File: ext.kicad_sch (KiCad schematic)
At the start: 41 parts, among them J4 0826-1X1T-GH-F, J8 Conn_01x02_Male, J9 Conn_01x02_Male, U10 LTC6820HMS, U11 LTC6820HMS, U12 LTC6820HMS, U13 AP1117-33, U9 LTC6820HMS

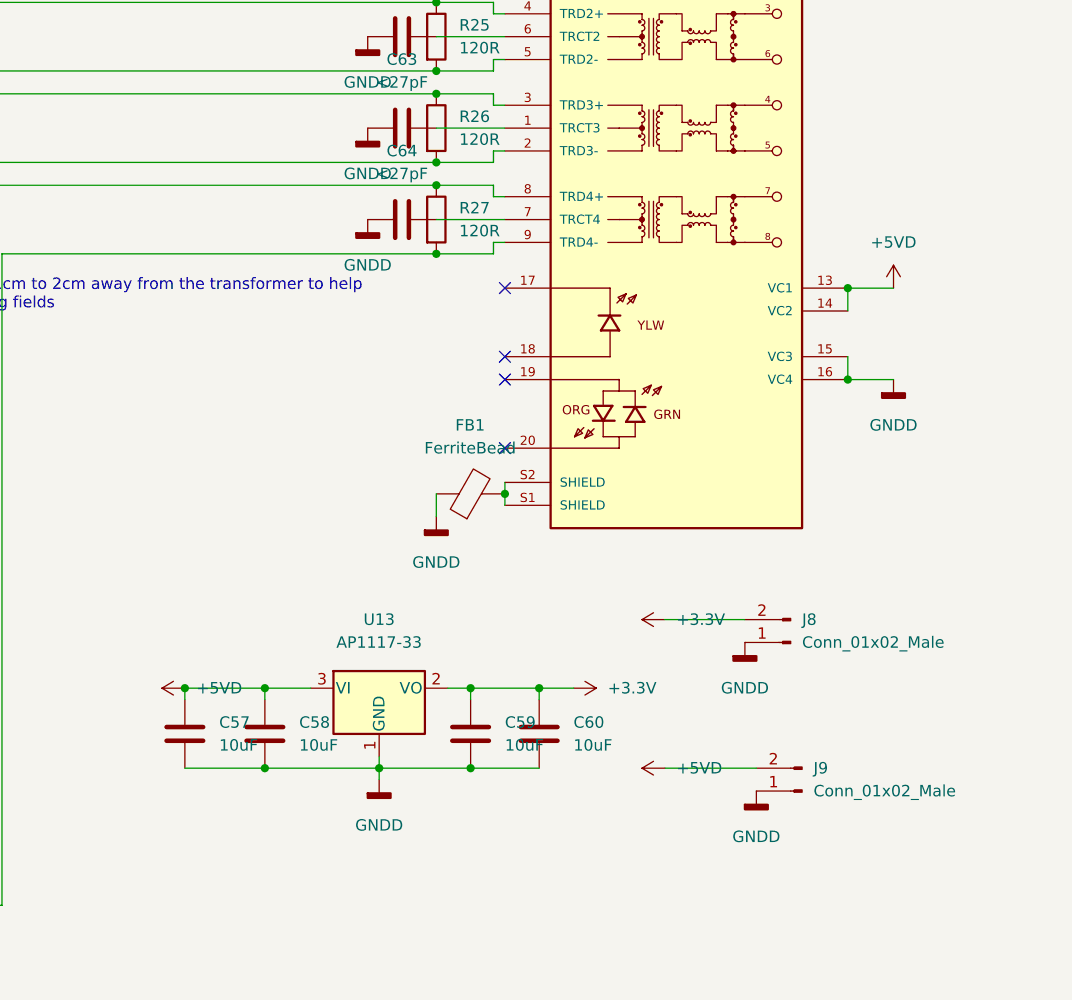
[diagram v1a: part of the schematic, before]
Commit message: remove 5V (now 3.3V) + tuning
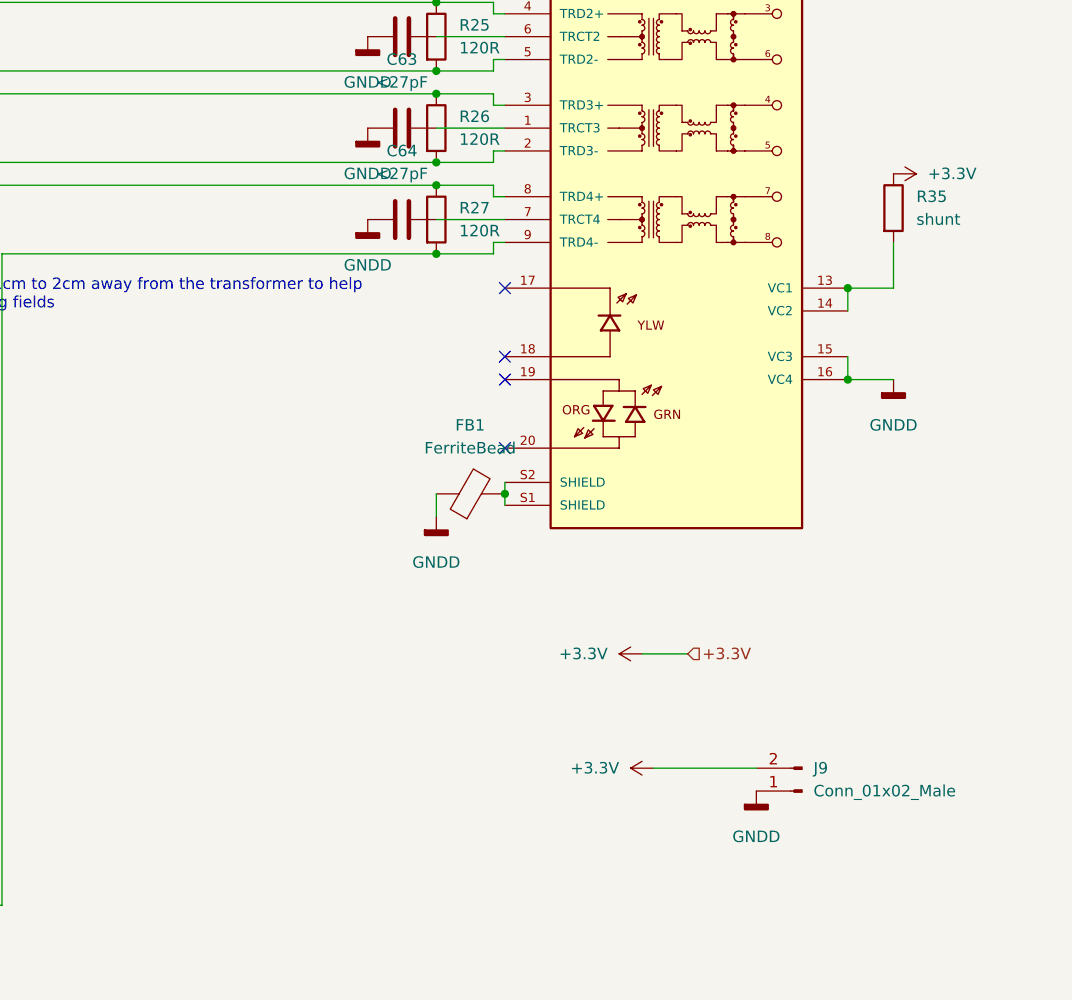
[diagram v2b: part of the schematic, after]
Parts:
- removed C57, C58, C59, C60: 10uF, Capacitor_SMD:C_1206_3216Metric, symbol Device:C
- removed J8: Conn_01x02_Male, Connector_Molex:Molex_KK-254_AE-6410-02A_1x02_P2.54mm_Vertical, symbol Connector:Conn_01x02_Male
- removed U13: AP1117-33, Package_TO_SOT_SMD:SOT-223-3_TabPin2, symbol Regulator_Linear:AZ1117-3.3
- added R35: shunt, Resistor_SMD:R_1210_3225Metric, symbol Device:R
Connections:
- net +3V3: now also J9.2 (Pin_2), R35.1
- net +5VD: no longer names the net of J4.13 (VC1), J4.14 (VC2)
- net +5VD: now also R35.2; no longer J9.2 (Pin_2)

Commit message: fix warnings
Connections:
- net +3V3 renamed power
